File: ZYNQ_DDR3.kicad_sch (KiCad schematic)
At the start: 3 parts, among them U1 XC7Z020-2CLG484I, U2 MT41K256M16TW-107:P, U3 MT41K256M16TW-107:P

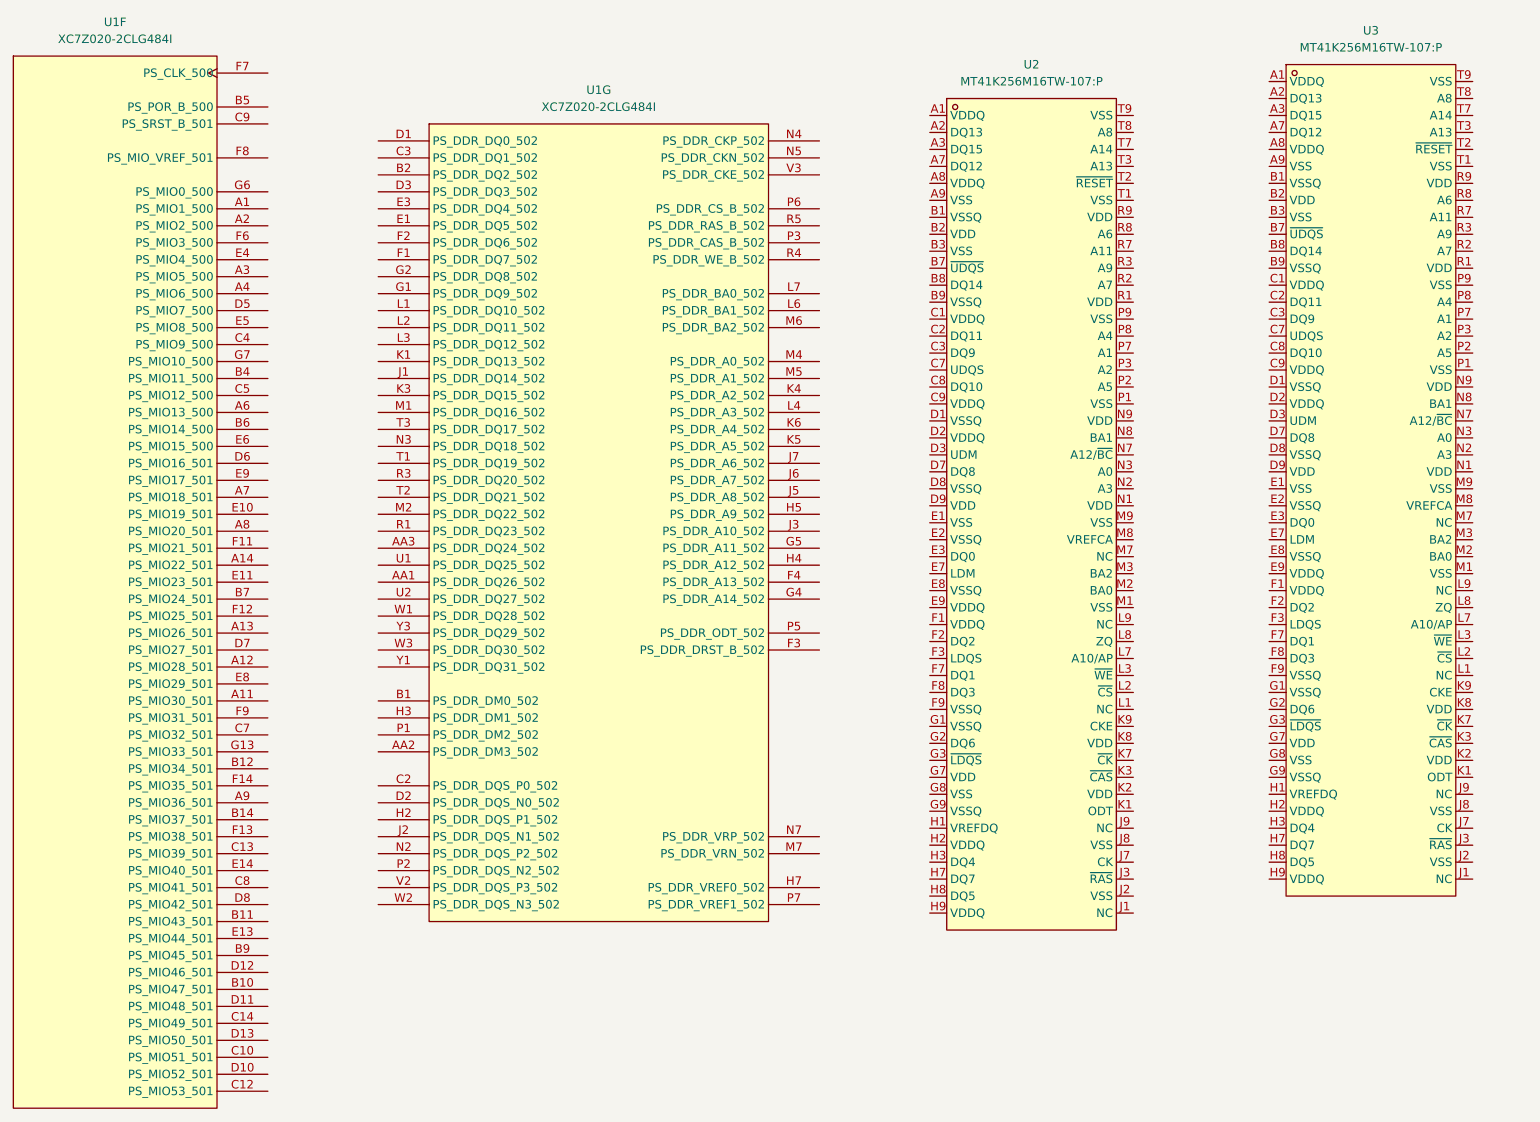
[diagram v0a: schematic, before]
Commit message: Refactor schematic hierarchy and add PL Ethernet
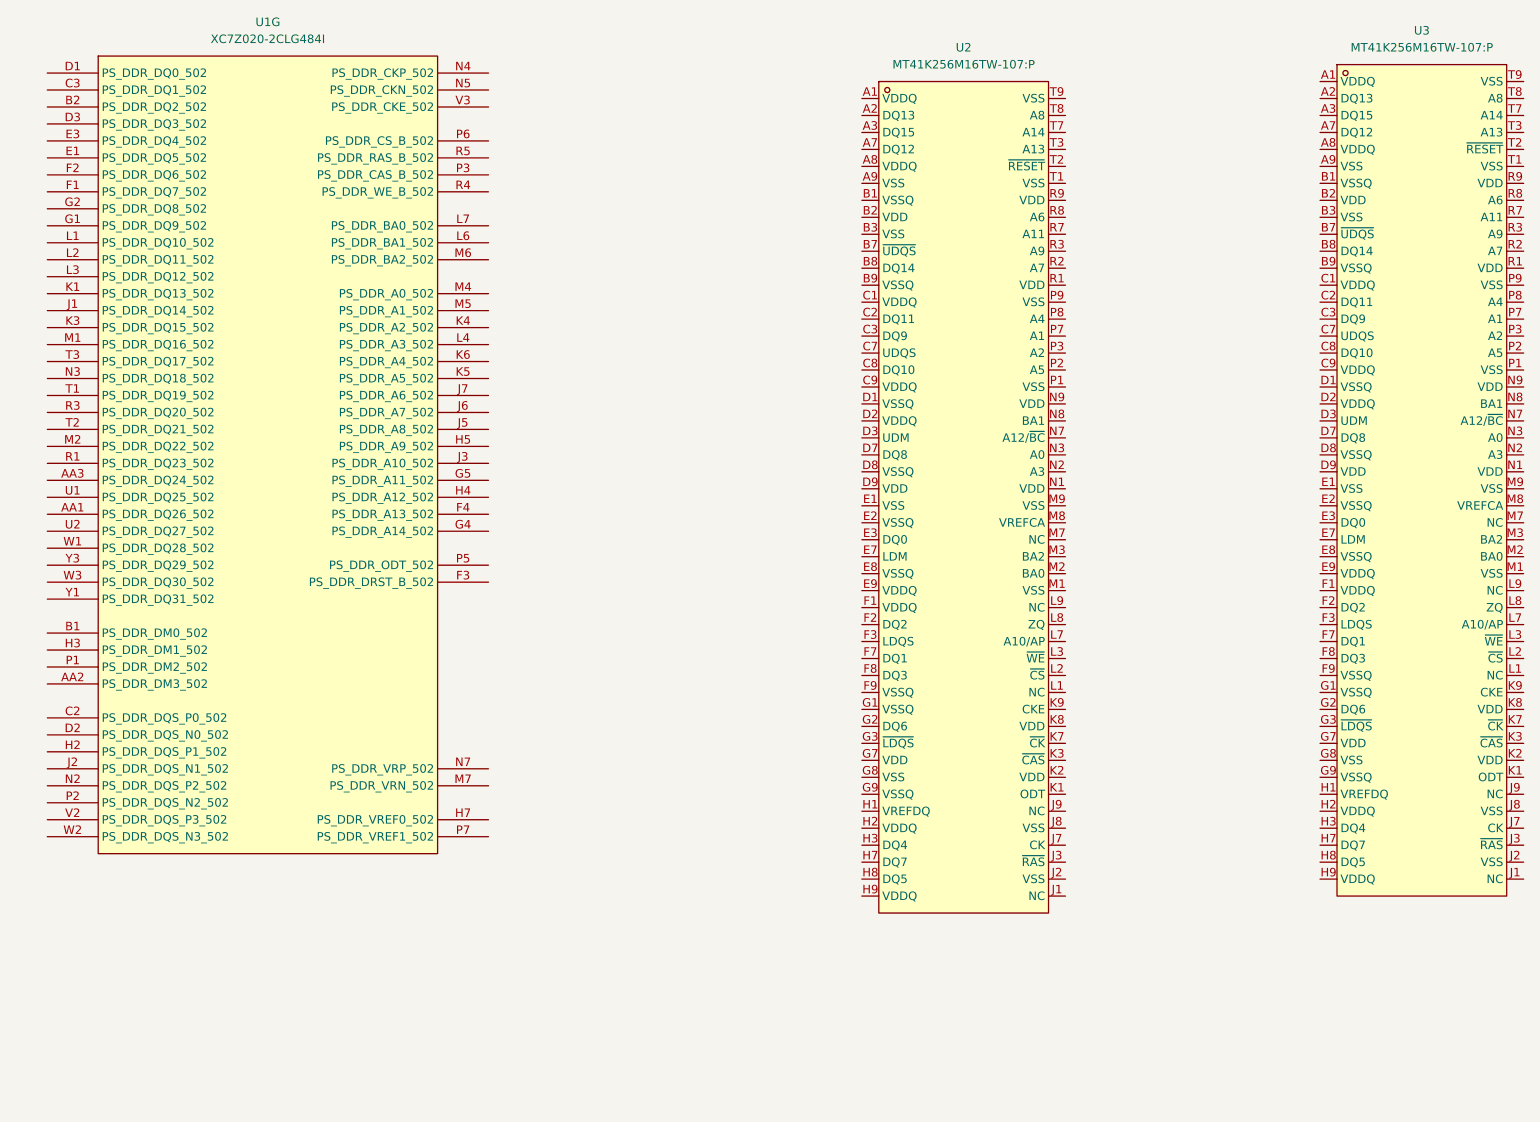
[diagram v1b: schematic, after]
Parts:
- removed unit 6 of U1
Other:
- moved on the sheet: U1G
